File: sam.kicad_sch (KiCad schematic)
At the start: 32 parts, among them IC4 74ACT02, IC5 74ACT138, IC6 74ACT138N, J1 JTAG, J3 Conn_01x24, J4 Conn_01x24, U3 XC95144XL-TQ100, X1 14.31818MHz

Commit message: complete initial routing
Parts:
- removed C12, C15: 100n, Capacitor_SMD:C_0805_2012Metric_Pad1.18x1.45mm_HandSolder, symbol Device:C
- removed U3: XC95144XL-TQ100, Package_QFP:TQFP-100_14x14mm_P0.5mm, symbol CPLD_Xilinx:XC95144XL-TQ100
- added C10, C13, C47, C52, C65, C70, C73, C74, C75, C76: 0.47uF, Capacitor_SMD:C_0805_2012Metric_Pad1.18x1.45mm_HandSolder, symbol Device:C_Small
- added C5, C59, C6, C60, C61, C62, C63, C64, C66, C67, C68, C69, C71, C72: 4.7uF, Capacitor_SMD:C_0805_2012Metric_Pad1.18x1.45mm_HandSolder, symbol Device:C_Small
- added R10, R11: 10K, Resistor_SMD:R_0805_2012Metric_Pad1.20x1.40mm_HandSolder, symbol Device:R
- added U3, U5: SN105125DBVR, Package_TO_SOT_SMD:SOT-23-5, symbol Regulator_Linear:TPS7A0533PDBV
- added U4: XC6SLX9-3TQG144I, Dragon:AMD-LQFP-144, symbol 6847:XC6SLX9-3TQG144I
- C11, C8: value 100n -> 1u; JLCPCB BOM 0 -> (none); LCSC Part C149620 -> C961513
- C7, C9: value 100n -> 1u; JLCPCB BOM 0 -> (none); LCSC Part C149620 -> C77080
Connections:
- net +3V3: now also C10.1, C13.1, C47.1, C5.1, C52.1, C6.1, C60.1, C62.1, C64.1, C66.1, C67.1, C68.1, C69.1, C70.1, C71.1, C72.1, C73.1, C74.1, C75.1, C76.1, U4.P103 (VCCO_1__2), U4.P122 (VCCO_0), U4.P125 (VCCO_0__1), U4.P129 (VCCAUX__4), U4.P135 (VCCO_0__2), U4.P18 (VCCO_3__1), U4.P20 (VCCAUX), U4.P31 (VCCO_3__2), U4.P36 (VCCAUX__1), U4.P4 (VCCO_3), U4.P42 (VCCO_2), U4.P53 (VCCAUX__2), U4.P63 (VCCO_2__1), U4.P76 (VCCO_1), U4.P86 (VCCO_1__1), U4.P90 (VCCAUX__3); no longer C11.1, C7.1, C8.1, C9.1
- net +5V: now also C7.1, C9.1, U3.1 (IN), U3.3 (EN), U5.1 (IN), U5.3 (EN)
- net A0: now also U4.P126 (IO_L36N_GCLK14_0)
- net A1: now also U4.P127 (IO_L36P_GCLK15_0)
- net A10: now also U4.P114 (IO_L65N_SCP2_0)
- net A11: now also U4.P115 (IO_L65P_SCP3_0)
- net A12: now also U4.P116 (IO_L64N_SCP4_0)
- net A13: now also U4.P117 (IO_L64P_SCP5_0)
- net A14: now also U4.P118 (IO_L63N_SCP6_0)
- net A15: now also U4.P119 (IO_L63P_SCP7_0)
- net A2: now also U4.P131 (IO_L35N_GCLK16_0)
- net A3: now also U4.P132 (IO_L35P_GCLK17_0)
- net A4: now also U4.P133 (IO_L34N_GCLK18_0)
- net A5: now also U4.P134 (IO_L34P_GCLK19_0)
- net A6: now also U4.P137 (IO_L4N_0)
- net A7: now also U4.P138 (IO_L4P_0)
- net A8: now also U4.P111 (IO_L66N_SCP0_0)
- net A9: now also U4.P112 (IO_L66P_SCP1_0)
- net D0: now also U4.P5 (IO_L52N_3)
- net D1: now also U4.P2 (IO_L83P_3)
- net D2: now also U4.P1 (IO_L83N_VREF_3)
- net D3: now also U4.P6 (IO_L52P_3)
- net D4: now also U4.P7 (IO_L51N_3)
- net D5: now also U4.P8 (IO_L51P_3)
- net D6: now also U4.P9 (IO_L50N_3)
- net D7: now also U4.P10 (IO_L50P_3)
- net DA0: now also U4.P124 (IO_L37P_GCLK13_0)
- net E: now also U4.P24 (IO_L41P_GCLK27_3)
- net GND: now also C10.2, C13.2, C47.2, C5.2, C52.2, C59.2, C6.2, C60.2, C61.2, C62.2, C63.2, C64.2, C65.2, C66.2, C67.2, C68.2, C69.2, C70.2, C71.2, C72.2, C73.2, C74.2, C75.2, C76.2, U3.2 (GND), U4.P108 (GND__9), U4.P113 (GND__10), U4.P13 (GND__1), U4.P130 (GND__11), U4.P136 (GND__12), U4.P25 (GND__2), U4.P3 (GND), U4.P49 (GND__3), U4.P54 (GND__4), U4.P68 (GND__5), U4.P77 (GND__6), U4.P91 (GND__7), U4.P96 (GND__8), U5.2 (GND)
- net OSC: now also U4.P123 (IO_L37N_GCLK12_0)
- net Q: now also U4.P23 (IO_L41N_GCLK26_3)
- net R/~{W}: now also U4.P66 (IO_L2N_CMPMOSI_2)
- net S0: now also U4.P139 (IO_L3N_0)
- net S1: now also U4.P140 (IO_L3P_0)
- net S2: now also U4.P141 (IO_L2N_0)
- net SZ0: now also U4.P67 (IO_L2P_CMPCLK_2)
- net SZ1: now also U4.P69 (IO_L1N_M0_CMPMISO_2)
- net SZ2: now also U4.P70 (IO_L1P_CCLK_2)
- net TCK: now also U4.P109 (TCK)
- net TDI0: now also U4.P106 (TDO)
- net TDI1: now also U4.P110 (TDI)
- net TMS: now also U4.P107 (TMS)
- net ~{FIRQx}: now also U4.P46 (IO_L49P_D3_2)
- net ~{FIRQ}: now also U4.P60 (IO_L13P_M1_2)
- net ~{IRQx}: now also U4.P45 (IO_L49N_D4_2)
- net ~{IRQ}: now also U4.P61 (IO_L12N_D2_MISO3_2)
- net ~{NHS}: now also U4.P65 (IO_L3P_D0_DIN_MISO_MISO1_2)
- net ~{NMIx}: now also U4.P47 (IO_L48N_RDWR_B_VREF_2)
- net ~{NMI}: now also U4.P62 (IO_L12P_D1_MISO2_2)
- net at R8.2: now also U4.P22 (IO_L42P_GCLK25_TRDY2_3)
- net zZ5: now reaches RN1.6
- net zZ5: now also U4.P88 (IO_L42P_GCLK7_1)
- net zZ13: now reaches RN2.6
- net zZ13: now also U4.P79 (IO_L47P_1)
- net zZ19: now reaches RN4.4
- net zZ19: now also U4.P100 (IO_L33P_1)
- net zZ18: now reaches RN4.3
- net zZ18: now also U4.P99 (IO_L33N_1)
- net zZ11: now reaches RN2.4
- net zZ11: now also U4.P81 (IO_L46P_1)
- net zZ10: now reaches RN2.3
- net zZ10: now also U4.P82 (IO_L45N_1)
- net zZ7: now reaches RN1.8
- net zZ7: now also U4.P85 (IO_L43P_GCLK5_1)
- net zZ17: now reaches RN4.2
- net zZ17: now also U4.P98 (IO_L34P_1)
- net zZ16: now reaches RN4.1
- net zZ16: now also U4.P74 (IO_L74N_DOUT_BUSY_1)
- net at R7.2: now also U4.P35 (IO_L1P_3)
- net zZ3: now reaches RN1.4
- net zZ3: now also U4.P93 (IO_L41P_GCLK9_IRDY1_1)
- net zZ21: now reaches RN4.6
- net zZ21: now also U4.P102 (IO_L32P_1)
- net zZ6: now reaches RN1.7
- net zZ6: now also U4.P87 (IO_L42N_GCLK6_TRDY1_1)
- net zZ8: now reaches RN2.1
- net zZ8: now also U4.P84 (IO_L43N_GCLK4_1)
- net zZ9: now reaches RN2.2
- net zZ9: now also U4.P83 (IO_L45P_1)
- net at R9.2: now also U4.P26 (IO_L37N_3)
- net zZ1: now reaches RN1.2
- net zZ1: now also U4.P95 (IO_L40P_GCLK11_1)
- net zZ15: now reaches RN2.8
- net zZ15: now also U4.P75 (IO_L74P_AWAKE_1)
- net zZ0: now reaches RN1.1
- net zZ0: now also U4.P97 (IO_L34N_1)
- net zZ20: now reaches RN4.5
- net zZ20: now also U4.P101 (IO_L32N_1)
- net zZ2: now reaches RN1.3
- net zZ2: now also U4.P94 (IO_L40N_GCLK10_1)
- net zZ12: now reaches RN2.5
- net zZ12: now also U4.P80 (IO_L46N_1)
- net zZ14: now reaches RN2.7
- net zZ14: now also U4.P78 (IO_L47N_1)
- net zZ4: now reaches RN1.5
- net zZ4: now also U4.P92 (IO_L41N_GCLK8_1)
- new net: R10.1, U3.4 (POK)
- new net: R11.1, U5.4 (POK)
- new net +1V2: C11.1, C59.1, C61.1, C63.1, C65.1, C8.1, R10.2, R11.2, U3.5 (OUT), U4.P128 (VCCINT__4), U4.P19 (VCCINT), U4.P28 (VCCINT__1), U4.P52 (VCCINT__2), U4.P89 (VCCINT__3), U5.5 (OUT)
- new net ~{RES}: U4.P64 (IO_L3N_MOSI_CSI_B_MISO0_2)
- no-connect marks 9 -> 41
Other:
- moved on the sheet: C14, IC4A, IC4B, IC4D, IC4E, IC5, IC6, J1, J3, J4, JP2, R12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

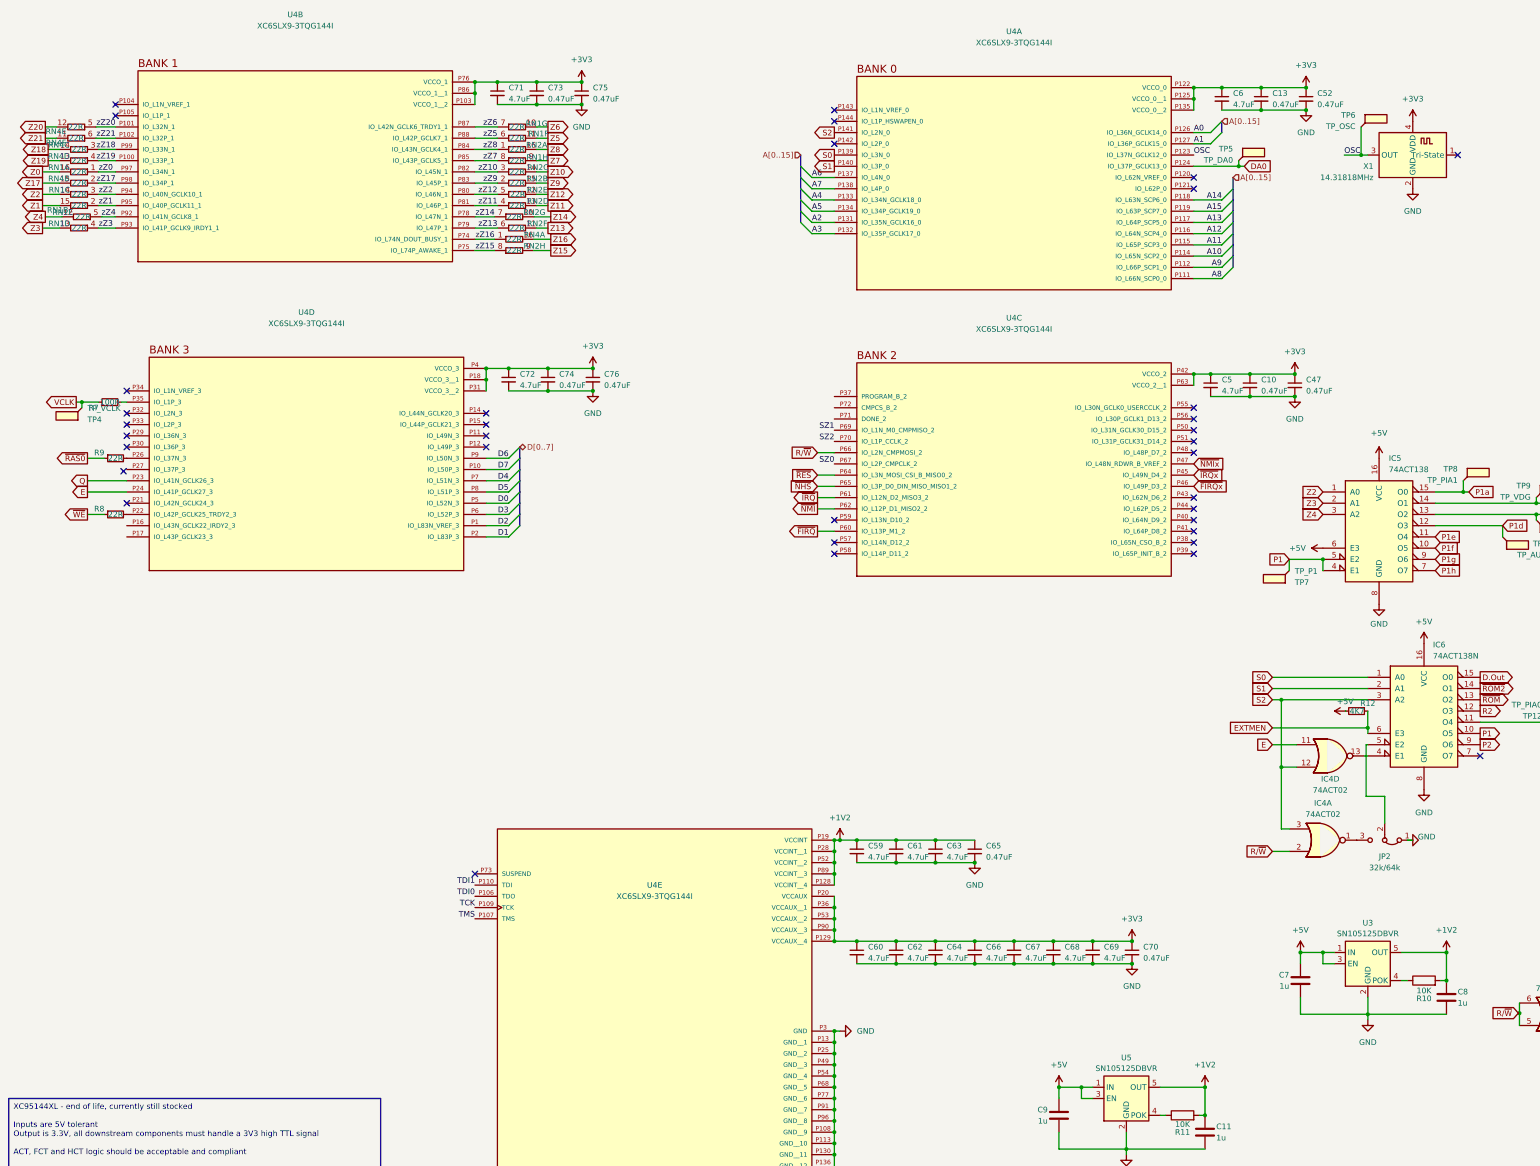
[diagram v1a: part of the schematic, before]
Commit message: add level shifting
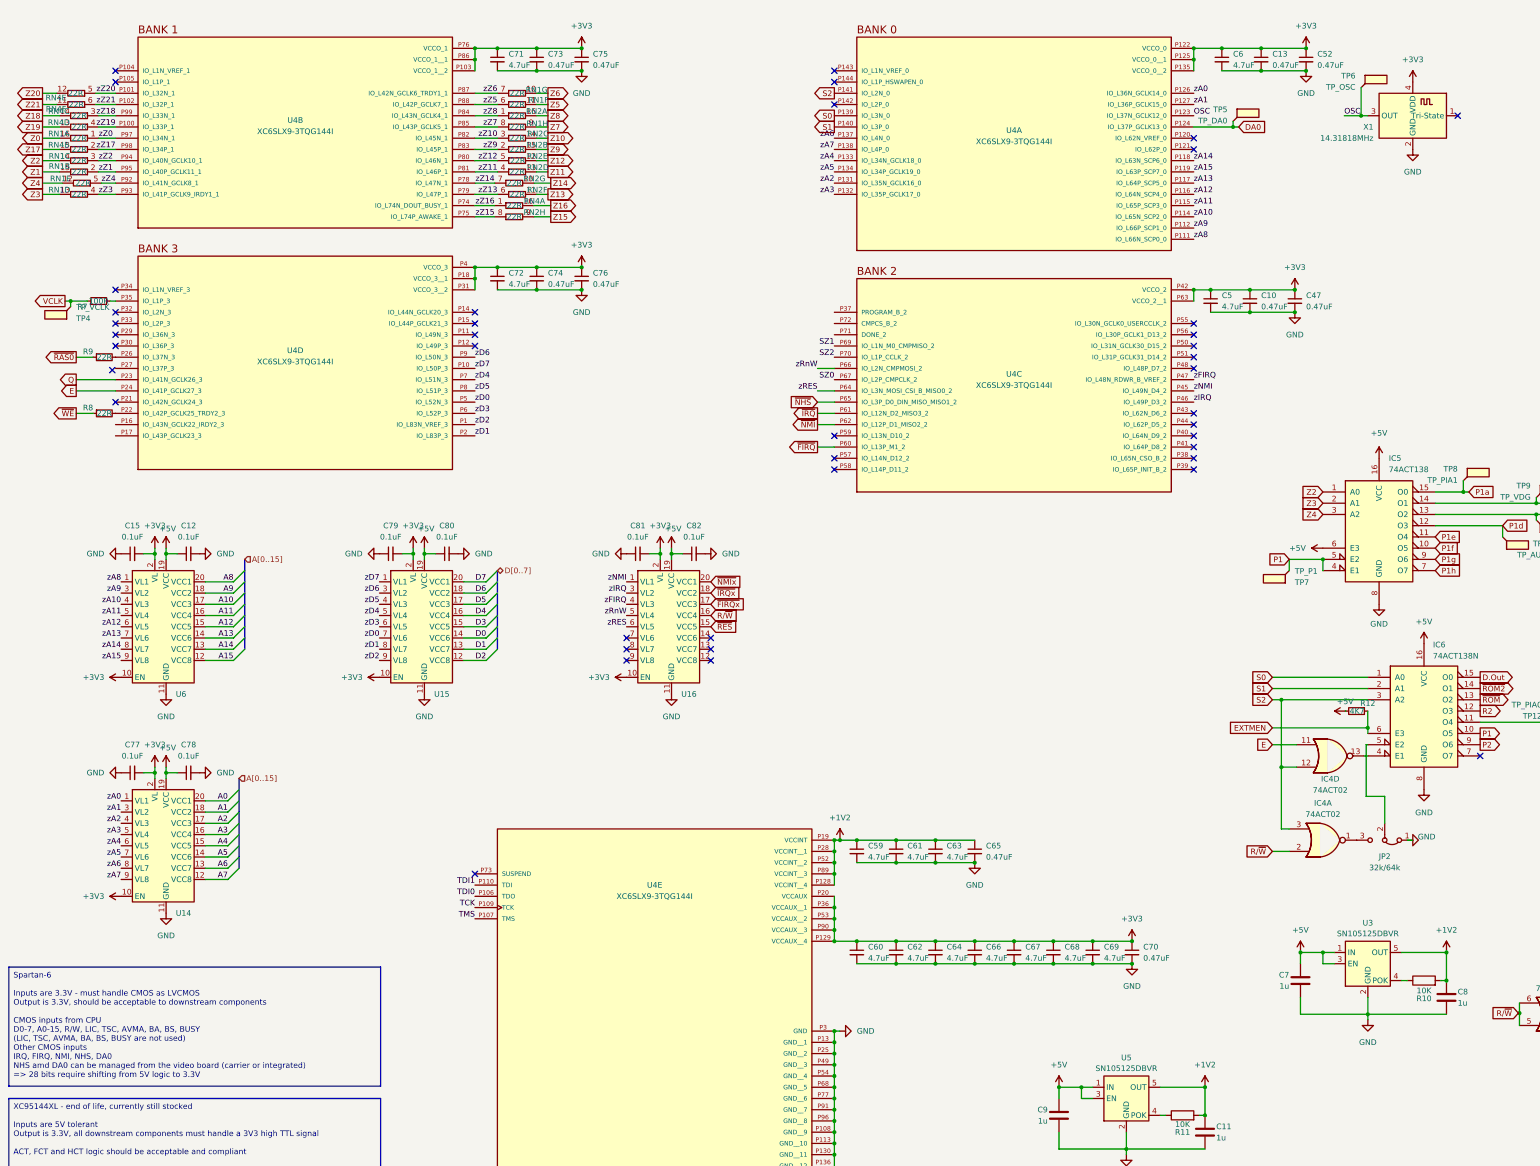
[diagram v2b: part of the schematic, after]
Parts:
- added C12, C15, C77, C78, C79, C80, C81, C82: 0.1uF, Capacitor_SMD:C_0805_2012Metric_Pad1.18x1.45mm_HandSolder, symbol Device:C_Small
- added U14, U15, U16, U6: ~, Package_SO:TSSOP-20_4.4x6.5mm_P0.65mm, symbol Motorola PIA:MAX3012
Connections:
- net +3V3: now also C15.2, C77.2, C79.2, C81.2, U14.10 (EN), U14.2 (VL), U15.10 (EN), U15.2 (VL), U16.10 (EN), U16.2 (VL), U6.10 (EN), U6.2 (VL)
- net +5V: now also C12.1, C78.1, C80.1, C82.1, U14.19 (VCC), U15.19 (VCC), U16.19 (VCC), U6.19 (VCC)
- net A0: now also U14.20 (VCC1); no longer U4.P126 (IO_L36N_GCLK14_0)
- net A1: now also U14.18 (VCC2); no longer U4.P127 (IO_L36P_GCLK15_0)
- net A10: now also U6.17 (VCC3); no longer U4.P114 (IO_L65N_SCP2_0)
- net A11: now also U6.16 (VCC4); no longer U4.P115 (IO_L65P_SCP3_0)
- net A12: now also U6.15 (VCC5); no longer U4.P116 (IO_L64N_SCP4_0)
- net A13: now also U6.14 (VCC6); no longer U4.P117 (IO_L64P_SCP5_0)
- net A14: now also U6.13 (VCC7); no longer U4.P118 (IO_L63N_SCP6_0)
- net A15: now also U6.12 (VCC8); no longer U4.P119 (IO_L63P_SCP7_0)
- net A2: now also U14.17 (VCC3); no longer U4.P131 (IO_L35N_GCLK16_0)
- net A3: now also U14.16 (VCC4); no longer U4.P132 (IO_L35P_GCLK17_0)
- net A4: now also U14.15 (VCC5); no longer U4.P133 (IO_L34N_GCLK18_0)
- net A5: now also U14.14 (VCC6); no longer U4.P134 (IO_L34P_GCLK19_0)
- net A6: now also U14.13 (VCC7); no longer U4.P137 (IO_L4N_0)
- net A7: now also U14.12 (VCC8); no longer U4.P138 (IO_L4P_0)
- net A8: now also U6.20 (VCC1); no longer U4.P111 (IO_L66N_SCP0_0)
- net A9: now also U6.18 (VCC2); no longer U4.P112 (IO_L66P_SCP1_0)
- net D0: now also U15.14 (VCC6); no longer U4.P5 (IO_L52N_3)
- net D1: now also U15.13 (VCC7); no longer U4.P2 (IO_L83P_3)
- net D2: now also U15.12 (VCC8); no longer U4.P1 (IO_L83N_VREF_3)
- net D3: now also U15.15 (VCC5); no longer U4.P6 (IO_L52P_3)
- net D4: now also U15.16 (VCC4); no longer U4.P7 (IO_L51N_3)
- net D5: now also U15.17 (VCC3); no longer U4.P8 (IO_L51P_3)
- net D6: now also U15.18 (VCC2); no longer U4.P9 (IO_L50N_3)
- net D7: now also U15.20 (VCC1); no longer U4.P10 (IO_L50P_3)
- net GND: now also C12.2, C15.1, C77.1, C78.2, C79.1, C80.2, C81.1, C82.2, U14.11 (GND), U15.11 (GND), U16.11 (GND), U6.11 (GND)
- net R/~{W}: now also U16.16 (VCC4); no longer U4.P66 (IO_L2N_CMPMOSI_2)
- net ~{FIRQx}: now also U16.17 (VCC3); no longer U4.P46 (IO_L49P_D3_2)
- net ~{IRQx}: now also U16.18 (VCC2); no longer U4.P45 (IO_L49N_D4_2)
- net ~{NMIx}: now also U16.20 (VCC1); no longer U4.P47 (IO_L48N_RDWR_B_VREF_2)
- net ~{RES}: now also U16.15 (VCC5); no longer U4.P64 (IO_L3N_MOSI_CSI_B_MISO0_2)
- net at U3.4 (POK): now also R10.1
- new net zA0: U14.1 (VL1), U4.P126 (IO_L36N_GCLK14_0)
- new net zA1: U14.3 (VL2), U4.P127 (IO_L36P_GCLK15_0)
- new net zA10: U4.P114 (IO_L65N_SCP2_0), U6.4 (VL3)
- new net zA11: U4.P115 (IO_L65P_SCP3_0), U6.5 (VL4)
- new net zA12: U4.P116 (IO_L64N_SCP4_0), U6.6 (VL5)
- new net zA13: U4.P117 (IO_L64P_SCP5_0), U6.7 (VL6)
- new net zA14: U4.P118 (IO_L63N_SCP6_0), U6.8 (VL7)
- new net zA15: U4.P119 (IO_L63P_SCP7_0), U6.9 (VL8)
- new net zA2: U14.4 (VL3), U4.P131 (IO_L35N_GCLK16_0)
- new net zA3: U14.5 (VL4), U4.P132 (IO_L35P_GCLK17_0)
- new net zA4: U14.6 (VL5), U4.P133 (IO_L34N_GCLK18_0)
- new net zA5: U14.7 (VL6), U4.P134 (IO_L34P_GCLK19_0)
- new net zA6: U14.8 (VL7), U4.P137 (IO_L4N_0)
- new net zA7: U14.9 (VL8), U4.P138 (IO_L4P_0)
- new net zA8: U4.P111 (IO_L66N_SCP0_0), U6.1 (VL1)
- new net zA9: U4.P112 (IO_L66P_SCP1_0), U6.3 (VL2)
- new net zD0: U15.7 (VL6), U4.P5 (IO_L52N_3)
- new net zD1: U15.8 (VL7), U4.P2 (IO_L83P_3)
- new net zD2: U15.9 (VL8), U4.P1 (IO_L83N_VREF_3)
- new net zD3: U15.6 (VL5), U4.P6 (IO_L52P_3)
- new net zD4: U15.5 (VL4), U4.P7 (IO_L51N_3)
- new net zD5: U15.4 (VL3), U4.P8 (IO_L51P_3)
- new net zD6: U15.3 (VL2), U4.P9 (IO_L50N_3)
- new net zD7: U15.1 (VL1), U4.P10 (IO_L50P_3)
- new net zFIRQ: U16.4 (VL3), U4.P47 (IO_L48N_RDWR_B_VREF_2)
- new net zIRQ: U16.3 (VL2), U4.P46 (IO_L49P_D3_2)
- new net zNMI: U16.1 (VL1), U4.P45 (IO_L49N_D4_2)
- new net zRES: U16.6 (VL5), U4.P64 (IO_L3N_MOSI_CSI_B_MISO0_2)
- new net zRnW: U16.5 (VL4), U4.P66 (IO_L2N_CMPMOSI_2)
- no-connect marks 41 -> 47
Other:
- moved on the sheet: C10, C13, C47, C5, C52, C6, C71, C72, C73, C74, C75, C76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
